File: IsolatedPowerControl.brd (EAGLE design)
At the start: 27.9 x 54.6 mm, 41 parts, among them Q1 FDN340P, Q2 FDN340P, U1 MCP23008-E/SO, U2 MCP4716A0T-E/CH, U3 MCP6273T-E/CH

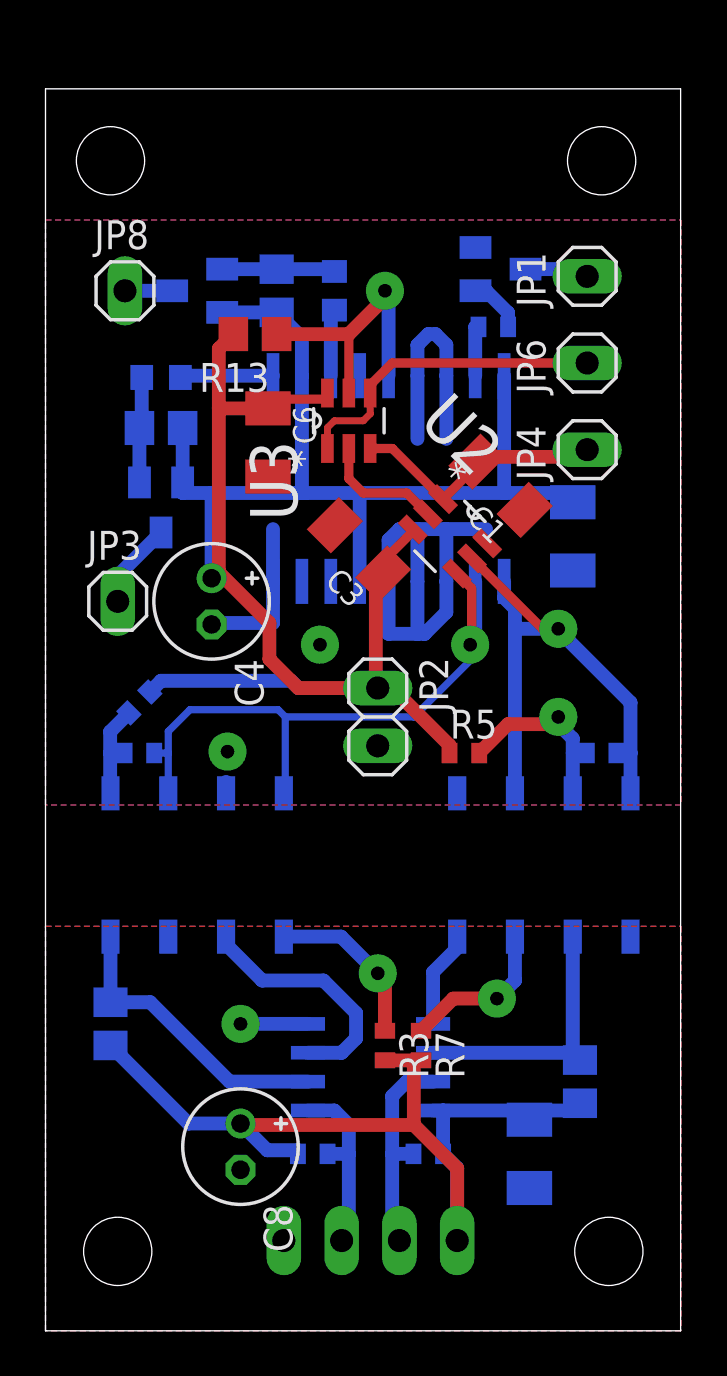
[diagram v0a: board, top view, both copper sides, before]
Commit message: Tweaks following etching to open up clearances
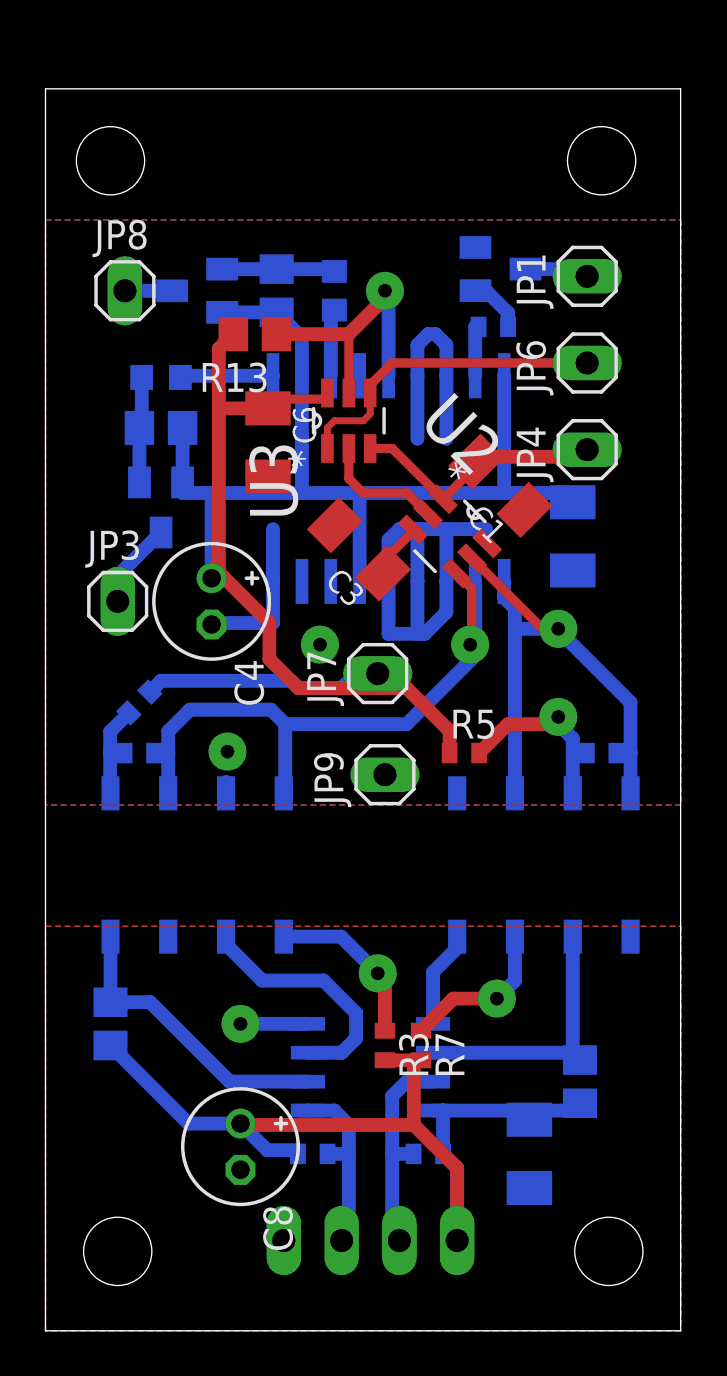
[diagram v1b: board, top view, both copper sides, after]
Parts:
- removed JP2: (no value), pinhead:1X02
- added JP7, JP9: (no value), pinhead:1X01-LARGEPAD
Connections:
- net V+: now also JP7.1; no longer JP2.1
- net V-: now also JP9.1; no longer JP2.2
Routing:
- net V+: track 94.0 -> 90.3 mm

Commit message: Added test software
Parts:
- R1, R10: value 2K2 -> 4K7
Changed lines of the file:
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@@
 <grid distance="0.025" unitdist="inch" unit="inch" style="lines" multiple="1" display="yes" altdistance="0.0125" altunitdist="inch" altunit="inch"/>
 <layers>
-<layer number="1" name="Top" color="4" fill="1" visible="yes" active="yes"/>
+<layer number="1" name="Top" color="4" fill="1" visible="no" active="yes"/>
 <layer number="2" name="Route2" color="1" fill="3" visible="no" active="no"/>
 <layer number="3" name="Route3" color="4" fill="3" visible="no" active="no"/>
@@
 <layer number="46" name="Milling" color="3" fill="1" visible="no" active="yes"/>
 <layer number="47" name="Measures" color="7" fill="1" visible="no" active="yes"/>
-<layer number="48" name="Document" color="7" fill="1" visible="no" active="yes"/>
+<layer number="48" name="Document" color="7" fill="1" visible="yes" active="yes"/>
 <layer number="49" name="Reference" color="7" fill="1" visible="no" active="yes"/>
 <layer number="50" name="dxf" color="7" fill="1" visible="no" active="no"/>
 <layer number="51" name="tDocu" color="7" fill="1" visible="no" active="yes"/>
-<layer number="52" name="bDocu" color="7" fill="1" visible="no" active="yes"/>
+<layer number="52" name="bDocu" color="7" fill="1" visible="yes" active="yes"/>
 <layer number="53" name="tGND_GNDA" color="7" fill="9" visible="no" active="no"/>
 <layer number="54" name="bGND_GNDA" color="1" fill="9" visible="no" active="no"/>
@@
 <element name="C6" library="rcl" package="C1206K" value="100n" x="9.779" y="39.0525" rot="R270"/>
 <element name="C8" library="rcl" package="E2-5" value="10uF" x="8.5725" y="8.09625" rot="R270"/>
-<element name="R1" library="rcl" package="R0402" value="2K2" x="16.8275" y="7.77875" rot="MR0"/>
-<element name="R10" library="rcl" package="R0402" value="2K2" x="11.7475" y="7.77875" rot="MR180"/>
+<element name="R1" library="rcl" package="R0402" value="4K7" x="16.8275" y="7.77875" rot="MR0"/>
+<element name="R10" library="rcl" package="R0402" value="4K7" x="11.7475" y="7.77875" rot="MR180"/>
 <element name="R11" library="rcl" package="R0402" value="4K7" x="19.685" y="44.1325" rot="MR180"/>
 <element name="R12" library="rcl" package="R0603" value="10" x="12.7" y="45.72" rot="MR270"/>

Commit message: Added documentation to schematic. Added STM32 test sketch
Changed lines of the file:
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@@
 <grid distance="0.025" unitdist="inch" unit="inch" style="lines" multiple="1" display="yes" altdistance="0.0125" altunitdist="inch" altunit="inch"/>
 <layers>
-<layer number="1" name="Top" color="4" fill="1" visible="no" active="yes"/>
+<layer number="1" name="Top" color="4" fill="1" visible="yes" active="yes"/>
 <layer number="2" name="Route2" color="1" fill="3" visible="no" active="no"/>
 <layer number="3" name="Route3" color="4" fill="3" visible="no" active="no"/>
@@
 <wire x1="10.1575" y1="43.815" x2="13.335" y2="43.815" width="0.6096" layer="1"/>
 <wire x1="13.335" y1="43.815" x2="14.9225" y2="45.4025" width="0.6096" layer="1"/>
-<wire x1="14.9225" y1="45.4025" x2="14.9225" y2="45.72" width="0.4064" layer="1"/>
+<wire x1="14.9225" y1="45.4025" x2="14.9225" y2="45.72" width="0.6096" layer="1"/>
 <wire x1="13.335" y1="41.2242" x2="13.335" y2="43.815" width="0.4064" layer="1"/>
 </signal>

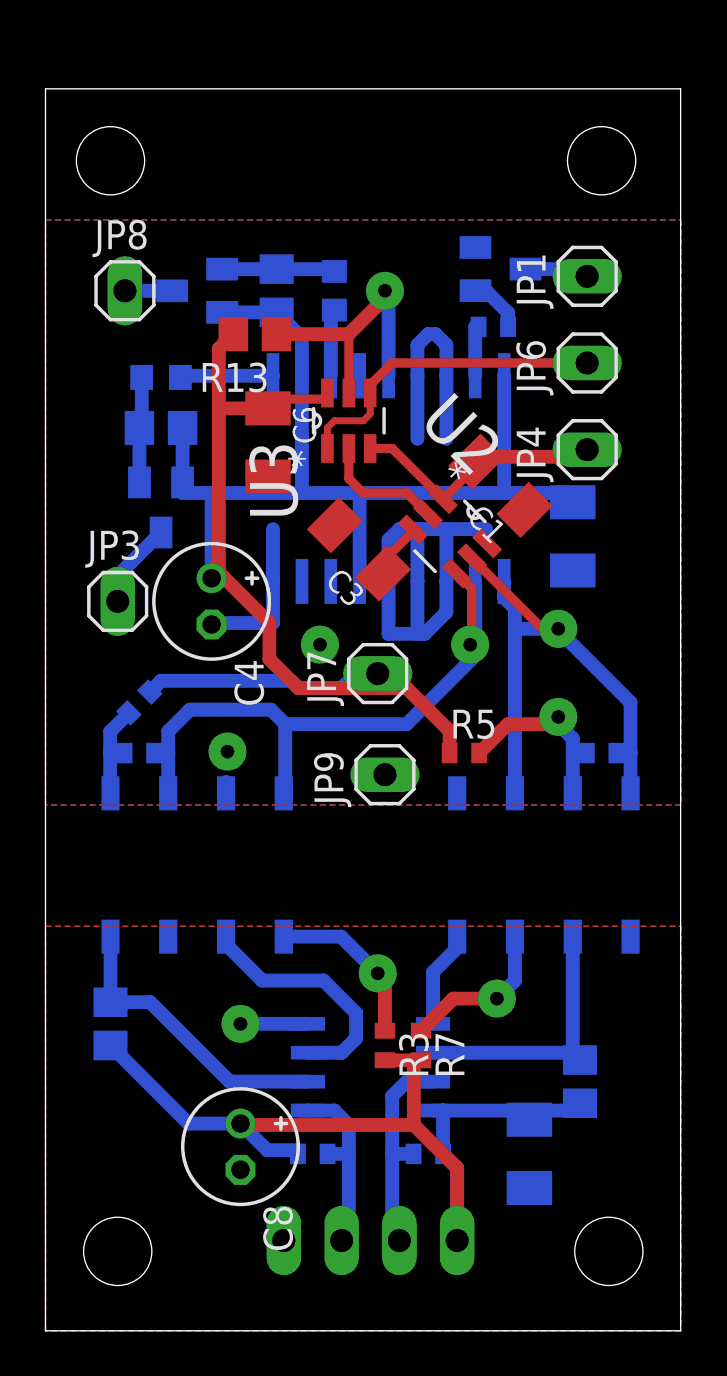
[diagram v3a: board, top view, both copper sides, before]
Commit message: Minor tweaks to the layout to line things up
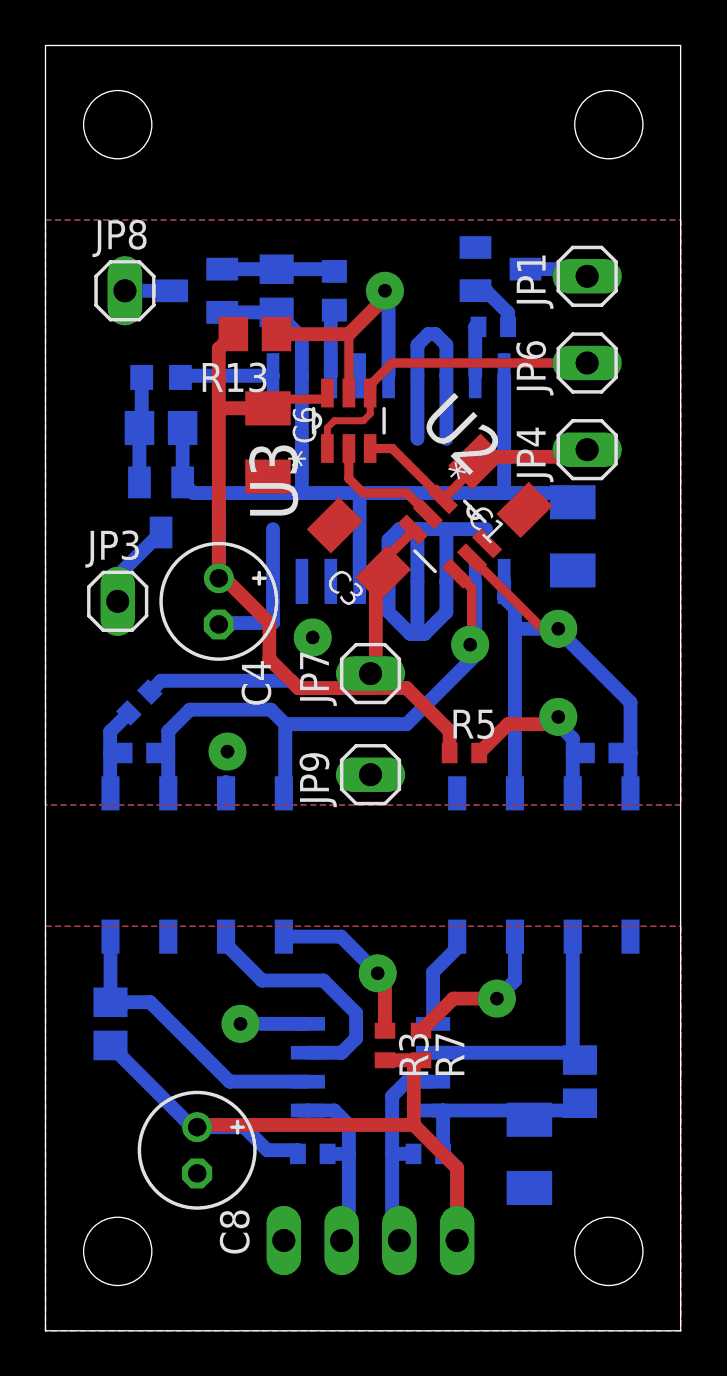
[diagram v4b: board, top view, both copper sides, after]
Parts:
- moved C8 1.91 mm to (6.67, 7.94)
- moved JP9 0.63 mm to (14.3, 24.4)
- moved JP7 0.32 mm to (14.3, 28.9)
- moved C4 0.32 mm to (7.62, 32.1)
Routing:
- net V+: track 90.3 -> 93.5 mm
- net +5V: track 42.4 -> 44.3 mm
- net V-: track 42.5 -> 41.7 mm
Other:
- board size 27.9 x 54.6 mm -> 27.9 x 56.5 mm
